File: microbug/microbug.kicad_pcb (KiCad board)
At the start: 2 copper layers, 31.7 x 38.1 mm, 25 parts, among them J1 Conn_01x03, J2 Conn_01x03, J3 Conn_01x02, M1 Motor_DC, M2 Motor_DC, U1 ATtiny1616-S, U2 QRE1113GR, U3 TC78H651AFNG, U4 QRE1113GR

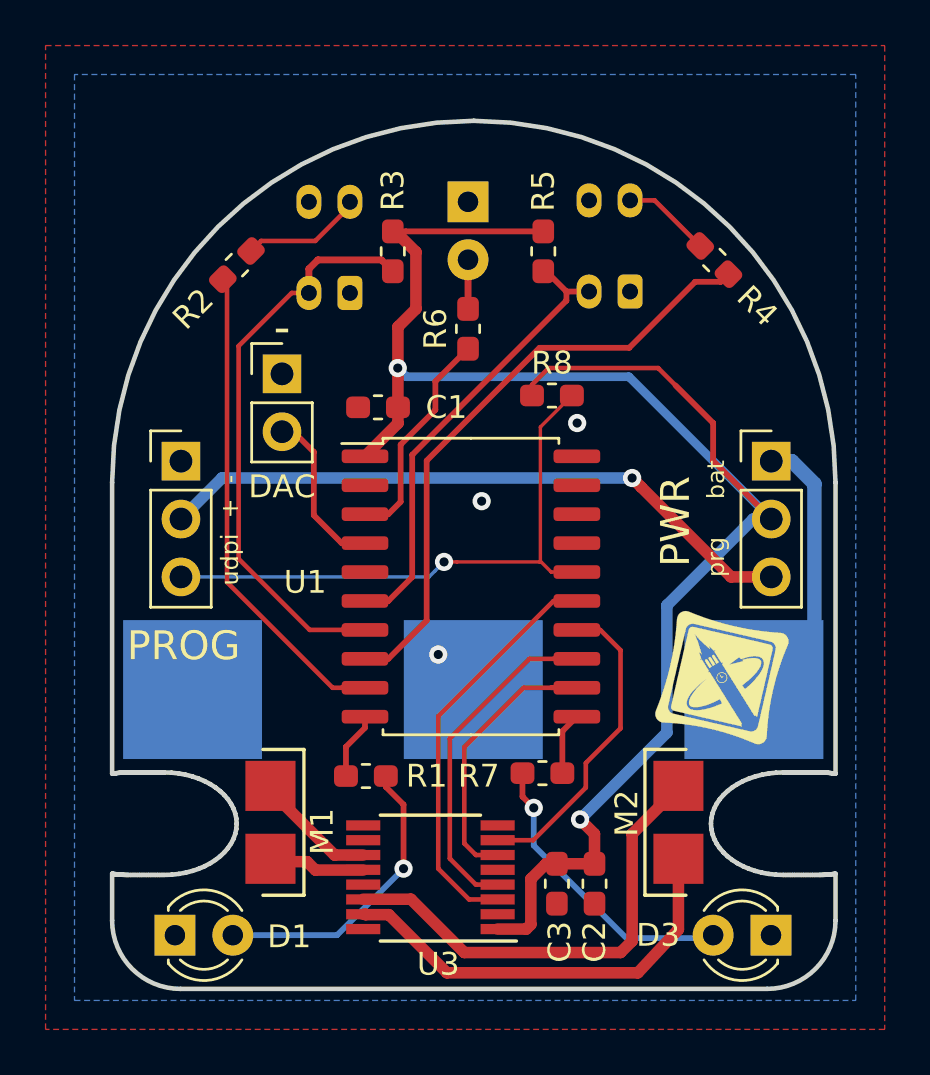
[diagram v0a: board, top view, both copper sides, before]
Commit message: Changed out motor driver, fixed various things (for reals) (#4)
* -> kicad v5.99 and added resistor for programming

* switched driver ic for 660

* added note

* fixed driver ic symbol name

* silkscreen stuff and added a via to connect ground planes

* fixed programming header stuff and qre111 symbol stuff

* pulled up mode pin

* pulled motor driver pin 15 up

Co-authored-by: Elam Day-Friedland <elamdf@berkeley.edu>
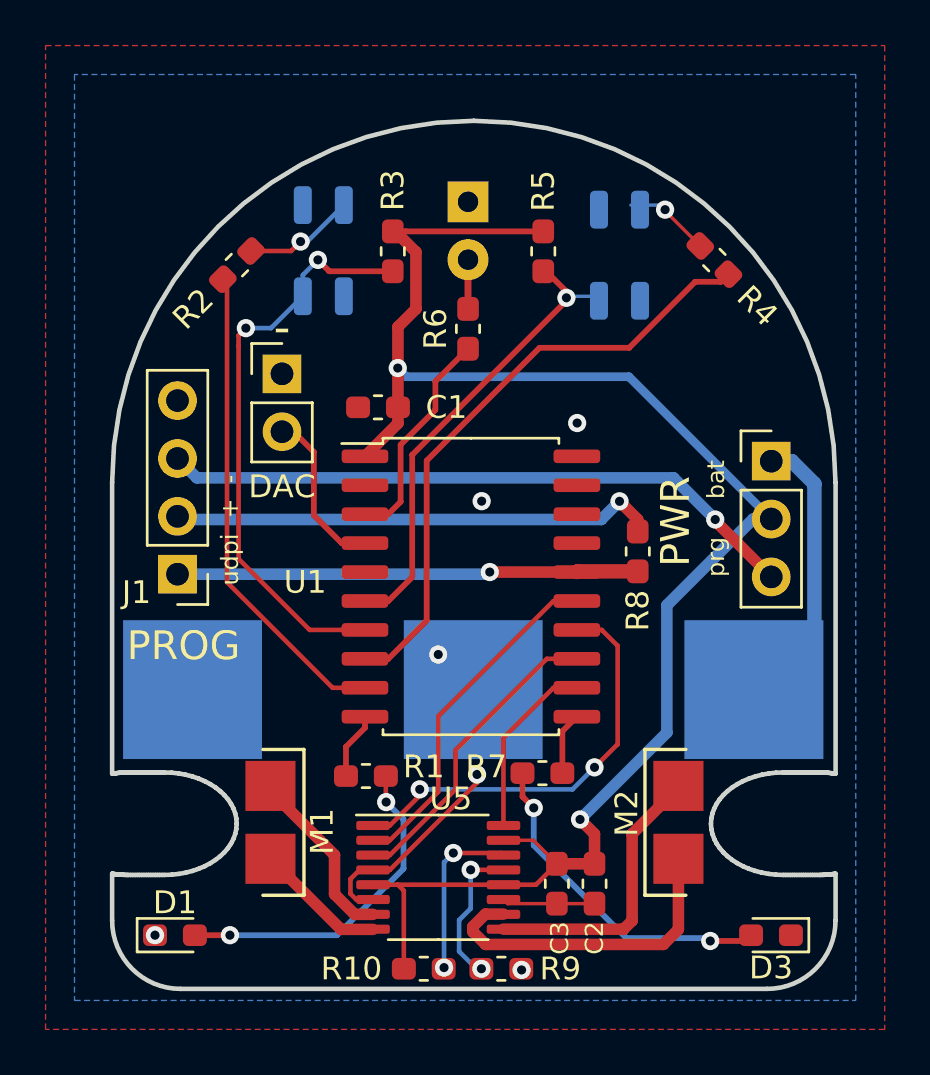
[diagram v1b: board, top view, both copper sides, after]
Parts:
- removed G***: LOGO, microbug-fplib:ieee-logo
- removed U4: QRE1113GR, OptoDevice:Everlight_ITR8307F43
- added R10: 10k, Resistor_SMD:R_0603_1608Metric_Pad1.05x0.95mm_HandSolder, F.Cu at (72.0, 74.1)
- added R9: 47k, Resistor_SMD:R_0603_1608Metric_Pad1.05x0.95mm_HandSolder, F.Cu at (75.4, 74.1)
- added U5: TC78H660FNG, Package_SO:TSSOP-16_4.4x5mm_P0.65mm, F.Cu at (72.6, 70.1)
- D1, D3: footprint LED_THT:LED_D3.0mm -> LED_SMD:LED_0603_1608Metric_Pad1.05x0.95mm_HandSolder
- J1: value Conn_01x03 -> Conn_01x04; footprint Connector_PinHeader_2.54mm:PinHeader_1x03_P2.54mm_Vertical -> Connector_PinHeader_2.54mm:PinHeader_1x04_P2.54mm_Vertical
- R8: value 10k -> 470
- U2: footprint OptoDevice:Everlight_ITR8307F43 -> OptoDevice:OnSemi_CASE100CY
- U3: value TC78H651AFNG -> QRE1113GR; footprint Package_SO:TSSOP-16_4.4x5mm_P0.65mm -> OptoDevice:OnSemi_CASE100CY; moved to B.Cu
- moved U3 28.5 mm to (80.6, 42.8)
- moved R8 7.81 mm to (81.4, 55.8), turned to -90 degrees
- moved J1 4.96 mm to (61.2, 56.8), turned to 180 degrees
- moved U2 2.19 mm to (67.6, 42.6)
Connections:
- J1 pad 1: GND -> /UDPI
- J1 pad 3: /UDPI -> Net-(J1-Pad3)
- J2 pad 3: Net-(J1-Pad2) -> Net-(J1-Pad3)
- R8 pad 1: +3V3 -> Net-(J1-Pad2)
- U1 pad 12: /PWM1 -> /PWM2
- U1 pad 13: /PWM2 -> /PWM1
- U1 pad 19: Net-(U1-Pad19) -> unconnected-(U1-Pad19)
- U1 pad 2: Net-(U1-Pad2) -> unconnected-(U1-Pad2)
- U1 pad 5: Net-(U1-Pad5) -> unconnected-(U1-Pad5)
- U2 pad 1: GND -> Net-(R2-Pad2)
- U2 pad 2: Net-(R2-Pad2) -> GND
- U3 pad 1: +3V3 -> Net-(R4-Pad2)
- U3 pad 2: Net-(U3-Pad2) -> GND
- U3 pad 3: /DIR2 -> /OUT2
- U3 pad 4: /PWM2 -> GND
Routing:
- net Net-(J1-Pad3): track 0.00 -> 28.2 mm, vias 0 -> 1
- net GND: track 0.00 -> 13.8 mm, vias 3 -> 6
- net Net-(M2-Pad2): track 20.6 -> 12.6 mm
- net /PWM2: track 15.9 -> 7.98 mm
- net Net-(R10-Pad2): track 0.00 -> 7.49 mm, vias 0 -> 2
- net Net-(J1-Pad2): track 28.5 -> 21.4 mm
- net Net-(R9-Pad2): track 0.00 -> 6.53 mm, vias 0 -> 2
- net /UDPI: track 25.7 -> 20.3 mm
- net /DIR1: track 13.8 -> 18.8 mm, vias 0 -> 2
- net +3V3: track 78.0 -> 73.0 mm
- net Net-(M2-Pad1): track 18.8 -> 14.4 mm
- net /DIR2: track 18.9 -> 16.1 mm
- net Net-(M1-Pad1): track 5.33 -> 7.85 mm
- net Net-(D3-Pad2): track 12.9 -> 14.9 mm, vias 1 -> 2
- net Net-(D1-Pad2): track 13.1 -> 14.8 mm, vias 1 -> 2
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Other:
- net class Default removed
